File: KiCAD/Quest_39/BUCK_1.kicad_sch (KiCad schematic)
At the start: 21 parts

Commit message: Fixed most ERC errors
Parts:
- gave numbers to parts that had none: 21
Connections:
- net Vin-: now also C33.2, R15.2, U9.9 (Vin-)
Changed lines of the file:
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@@
     (effects (font (size 1.27 1.27)) (justify left bottom))
   )
-  (label "Vin-" (at 62.23 78.74 0)
+  (label "Vin-" (at 63.5 78.74 0)
     (effects (font (size 1.27 1.27)) (justify left bottom))
   )
@@
   (symbol (lib_id "Device:C") (at 127 137.16 0) (unit 1)
     (in_bom yes) (on_board yes) (fields_autoplaced)
-    (property "Reference" "C?" (id 0) (at 130.81 135.8899 0)
+    (property "Reference" "C34" (id 0) (at 130.81 135.8899 0)
       (effects (font (size 1.27 1.27)) (justify left))
     )
@@
   (symbol (lib_id "power:+5V") (at 77.47 59.69 0) (unit 1)
     (in_bom yes) (on_board yes) (fields_autoplaced)
-    (property "Reference" "#PWR0120" (id 0) (at 77.47 63.5 0)
+    (property "Reference" "#PWR015" (id 0) (at 77.47 63.5 0)
       (effects (font (size 1.27 1.27)) hide)
     )
@@
   (symbol (lib_id "Device:C_Polarized") (at 85.09 46.99 0) (unit 1)
     (in_bom yes) (on_board yes) (fields_autoplaced)
-    (property "Reference" "C?" (id 0) (at 88.9 44.8309 0)
+    (property "Reference" "C29" (id 0) (at 88.9 44.8309 0)
       (effects (font (size 1.27 1.27)) (justify left))
     )
@@
   (symbol (lib_id "Device:R") (at 46.99 49.53 0) (unit 1)
     (in_bom yes) (on_board yes) (fields_autoplaced)
-    (property "Reference" "R?" (id 0) (at 49.53 48.2599 0)
+    (property "Reference" "R14" (id 0) (at 49.53 48.2599 0)
       (effects (font (size 1.27 1.27)) (justify left))
     )
@@
   (symbol (lib_id "Amplifier_Operational:MCP601-xOT") (at 34.29 66.04 0) (unit 1)
     (in_bom yes) (on_board yes)
-    (property "Reference" "U?" (id 0) (at 36.83 62.23 0))
+    (property "Reference" "U8" (id 0) (at 36.83 62.23 0))
     (property "Value" "MCP601T-I/OT" (id 1) (at 40.64 69.85 0))
     (property "Footprint" "Package_TO_SOT_SMD:SOT-23-5" (id 2) (at 31.75 71.12 0)
@@
   (symbol (lib_id "power:GND") (at 281.94 229.87 0) (unit 1)
     (in_bom yes) (on_board yes) (fields_autoplaced)
-    (property "Reference" "#PWR0117" (id 0) (at 281.94 236.22 0)
+    (property "Reference" "#PWR019" (id 0) (at 281.94 236.22 0)
       (effects (font (size 1.27 1.27)) hide)
     )
@@
   (symbol (lib_id "power:+5V") (at 336.55 218.44 0) (unit 1)
     (in_bom yes) (on_board yes) (fields_autoplaced)
-    (property "Reference" "#PWR0118" (id 0) (at 336.55 222.25 0)
+    (property "Reference" "#PWR018" (id 0) (at 336.55 222.25 0)
       (effects (font (size 1.27 1.27)) hide)
     )
@@
   (symbol (lib_id "Device:C") (at 99.06 46.99 0) (unit 1)
     (in_bom yes) (on_board yes) (fields_autoplaced)
-    (property "Reference" "C?" (id 0) (at 102.87 45.7199 0)
+    (property "Reference" "C30" (id 0) (at 102.87 45.7199 0)
       (effects (font (size 1.27 1.27)) (justify left))
     )
@@
   (symbol (lib_id "Device:C_Polarized") (at 353.06 172.72 0) (unit 1)
     (in_bom yes) (on_board yes)
-    (property "Reference" "C?" (id 0) (at 356.8495 171.4075 0)
+    (property "Reference" "C36" (id 0) (at 356.8495 171.4075 0)
       (effects (font (size 1.27 1.27)) (justify left))
     )
@@
   (symbol (lib_id "power:+5V") (at 31.75 57.15 0) (unit 1)
     (in_bom yes) (on_board yes) (fields_autoplaced)
-    (property "Reference" "#PWR0121" (id 0) (at 31.75 60.96 0)
+    (property "Reference" "#PWR014" (id 0) (at 31.75 60.96 0)
       (effects (font (size 1.27 1.27)) hide)
     )
@@
   (symbol (lib_id "Device:C") (at 54.61 55.88 90) (unit 1)
     (in_bom yes) (on_board yes)
-    (property "Reference" "C?" (id 0) (at 54.61 52.07 90))
+    (property "Reference" "C33" (id 0) (at 54.61 52.07 90))
     (property "Value" "1uF" (id 1) (at 54.61 59.69 90))
     (property "Footprint" "OptoDevice:R_LDR_4.9x4.2mm_P2.54mm_Vertical" (id 2) (at 58.42 54.9148 0)
@@
   (symbol (lib_id "Device:R") (at 125.73 91.44 0) (unit 1)
     (in_bom yes) (on_board yes) (fields_autoplaced)
-    (property "Reference" "R?" (id 0) (at 128.27 90.1699 0)
+    (property "Reference" "R16" (id 0) (at 128.27 90.1699 0)
       (effects (font (size 1.27 1.27)) (justify left))
     )
@@
   (symbol (lib_id "Device:R") (at 321.31 215.9 0) (unit 1)
     (in_bom yes) (on_board yes) (fields_autoplaced)
-    (property "Reference" "R?" (id 0) (at 323.85 214.6299 0)
+    (property "Reference" "R17" (id 0) (at 323.85 214.6299 0)
       (effects (font (size 1.27 1.27)) (justify left))
     )
@@
   (symbol (lib_id "Device:C_Polarized") (at 367.03 172.72 0) (unit 1)
     (in_bom yes) (on_board yes)
-    (property "Reference" "C?" (id 0) (at 370.8195 171.4075 0)
+    (property "Reference" "C37" (id 0) (at 370.8195 171.4075 0)
       (effects (font (size 1.27 1.27)) (justify left))
     )
@@
   (symbol (lib_id "LTM4611EV:LTM4611EV-PBF") (at 130.81 102.87 0) (unit 1)
     (in_bom yes) (on_board yes)
-    (property "Reference" "U?" (id 0) (at 307.34 50.8 0)
+    (property "Reference" "U10" (id 0) (at 307.34 50.8 0)
       (effects (font (size 1.524 1.524)))
     )
@@
   (symbol (lib_id "Device:R") (at 54.61 41.91 90) (unit 1)
     (in_bom yes) (on_board yes) (fields_autoplaced)
-    (property "Reference" "R?" (id 0) (at 54.61 35.56 90))
+    (property "Reference" "R13" (id 0) (at 54.61 35.56 90))
     (property "Value" "0R0025" (id 1) (at 54.61 38.1 90))
     (property "Footprint" "" (id 2) (at 54.61 43.688 90)
@@
   (symbol (lib_id "Analog_ADC:INA226") (at 77.47 73.66 0) (unit 1)
     (in_bom yes) (on_board yes)
-    (property "Reference" "U?" (id 0) (at 82.55 62.23 0)
+    (property "Reference" "U9" (id 0) (at 82.55 62.23 0)
       (effects (font (size 1.27 1.27)) (justify left))
     )
@@
   (symbol (lib_id "Device:C") (at 336.55 224.79 0) (unit 1)
     (in_bom yes) (on_board yes) (fields_autoplaced)
-    (property "Reference" "C?" (id 0) (at 340.36 223.5199 0)
+    (property "Reference" "C40" (id 0) (at 340.36 223.5199 0)
       (effects (font (size 1.27 1.27)) (justify left))
     )
@@
   (symbol (lib_id "power:GND") (at 31.75 76.2 0) (unit 1)
     (in_bom yes) (on_board yes) (fields_autoplaced)
-    (property "Reference" "#PWR0123" (id 0) (at 31.75 82.55 0)
+    (property "Reference" "#PWR016" (id 0) (at 31.75 82.55 0)
       (effects (font (size 1.27 1.27)) hide)
     )
@@
   (symbol (lib_id "Device:R") (at 59.69 49.53 0) (unit 1)
     (in_bom yes) (on_board yes) (fields_autoplaced)
-    (property "Reference" "R?" (id 0) (at 62.23 48.2599 0)
+    (property "Reference" "R15" (id 0) (at 62.23 48.2599 0)
       (effects (font (size 1.27 1.27)) (justify left))
     )
@@
   (symbol (lib_id "power:GND") (at 100.33 87.63 0) (unit 1)
     (in_bom yes) (on_board yes) (fields_autoplaced)
-    (property "Reference" "#PWR0122" (id 0) (at 100.33 93.98 0)
+    (property "Reference" "#PWR017" (id 0) (at 100.33 93.98 0)
       (effects (font (size 1.27 1.27)) hide)
     )
@@
   (symbol (lib_id "MCP4151:MCP4151-502E{slash}SN") (at 252.73 220.98 0) (unit 1)
     (in_bom yes) (on_board yes)
-    (property "Reference" "U?" (id 0) (at 311.15 214.63 0)
+    (property "Reference" "U11" (id 0) (at 311.15 214.63 0)
       (effects (font (size 1.524 1.524)))
     )
@@
   (symbol (lib_id "Device:C_Polarized") (at 379.73 172.72 0) (unit 1)
     (in_bom yes) (on_board yes)
-    (property "Reference" "C?" (id 0) (at 383.5195 171.4075 0)
+    (property "Reference" "C38" (id 0) (at 383.5195 171.4075 0)
       (effects (font (size 1.27 1.27)) (justify left))
     )
@@
   (symbol (lib_id "Device:C") (at 111.76 46.99 0) (unit 1)
     (in_bom yes) (on_board yes) (fields_autoplaced)
-    (property "Reference" "C?" (id 0) (at 115.57 45.7199 0)
+    (property "Reference" "C31" (id 0) (at 115.57 45.7199 0)
       (effects (font (size 1.27 1.27)) (justify left))
     )
@@
   (symbol (lib_id "Device:C") (at 334.01 172.72 0) (unit 1)
     (in_bom yes) (on_board yes) (fields_autoplaced)
-    (property "Reference" "C?" (id 0) (at 337.82 171.4499 0)
+    (property "Reference" "C35" (id 0) (at 337.82 171.4499 0)
       (effects (font (size 1.27 1.27)) (justify left))
     )
@@
   (symbol (lib_id "Device:C_Polarized") (at 392.43 172.72 0) (unit 1)
     (in_bom yes) (on_board yes)
-    (property "Reference" "C?" (id 0) (at 396.2195 171.4075 0)
+    (property "Reference" "C39" (id 0) (at 396.2195 171.4075 0)
       (effects (font (size 1.27 1.27)) (justify left))
     )
@@
   (symbol (lib_id "power:GND") (at 336.55 229.87 0) (unit 1)
     (in_bom yes) (on_board yes) (fields_autoplaced)
-    (property "Reference" "#PWR0119" (id 0) (at 336.55 236.22 0)
+    (property "Reference" "#PWR020" (id 0) (at 336.55 236.22 0)
       (effects (font (size 1.27 1.27)) hide)
     )
@@
   (symbol (lib_id "Device:C") (at 124.46 46.99 0) (unit 1)
     (in_bom yes) (on_board yes) (fields_autoplaced)
-    (property "Reference" "C?" (id 0) (at 128.27 45.7199 0)
-      (effects (font (size 1.27 1.27)) (justify left))
-    )
+    (property "Reference" "C32" (id 0) (at 128.27 45.7199 0)
+      (effects (font (size 1.27 1.27)) (justify left))
+    )

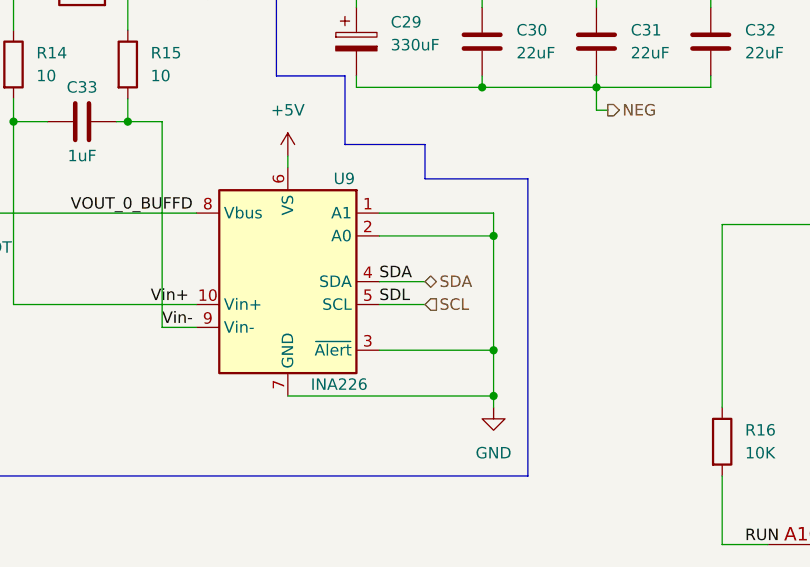
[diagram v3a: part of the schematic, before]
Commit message: Added weak SPI CS pullups to prevent spurious behaviour
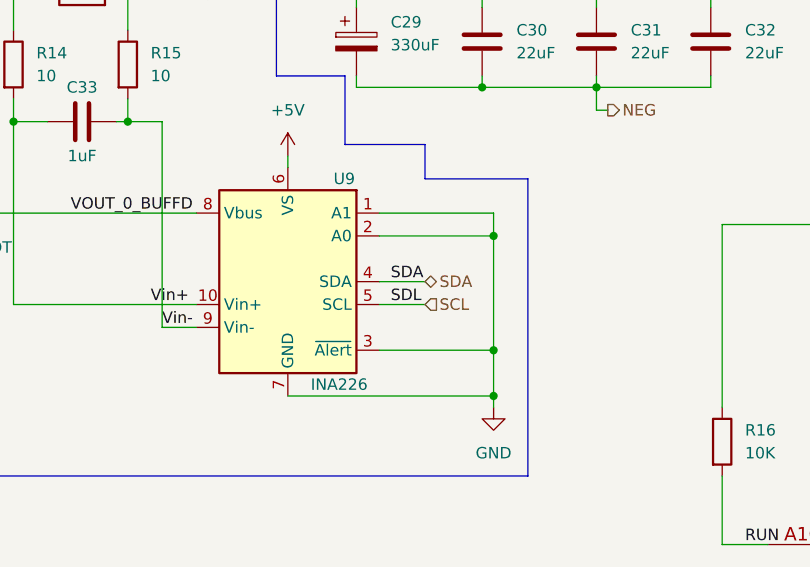
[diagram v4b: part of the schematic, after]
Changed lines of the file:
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@@
+    (effects (font (size 1.27 1.27)) (justify left bottom))
+  )
+  (label "SDA" (at 88.9 73.66 0)
     (effects (font (size 1.27 1.27)) (justify left bottom))
   )
@@
     (effects (font (size 1.27 1.27)) (justify left bottom))
   )
-  (label "SDL" (at 87.63 76.2 0)
+  (label "VOUT_0_BUFFD" (at 53.34 66.04 0)
     (effects (font (size 1.27 1.27)) (justify left bottom))
   )
-  (label "VOUT_0_BUFFD" (at 53.34 66.04 0)
+  (label "SDL" (at 88.9 76.2 0)
     (effects (font (size 1.27 1.27)) (justify left bottom))
   )
@@
     (effects (font (size 1.27 1.27)) (justify left bottom))
   )
-  (label "SDA" (at 87.63 73.66 0)
-    (effects (font (size 1.27 1.27)) (justify left bottom))
-  )

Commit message: Gave all INA226's unique addresses
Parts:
- removed C29: 330uF, symbol Device:C_Polarized
- removed R13: 0R0025, symbol Device:R
- removed R14, R15: 10, symbol Device:R
- removed R16: 10K, symbol Device:R
- removed R17: 20K, symbol Device:R
- removed U8: MCP601T-I/OT, Package_TO_SOT_SMD:SOT-23-5, symbol Amplifier_Operational:MCP601-xOT
- added C28: 330uF, symbol Device:C_Polarized
- added C29: 22uF, symbol Device:C
- added C41: 100nF, symbol Device:C
- added R24: 0R0025, symbol Device:R
- added R25, R26: 10R, symbol Device:R
- added R27: 9k, symbol Device:R
- added R28: 1k, symbol Device:R
- added R29: 10k, symbol Device:R
- added R30: 20K, symbol Device:R
- added TP13, TP14, TP15, TP16, TP17, TP18, TP19: TestPoint, symbol Connector:TestPoint
- added U8: AD626ANZ, N_8_ADI, symbol AD626ANZ:AD626ANZ
- C32: value 22uF -> 1uF; footprint (none) -> OptoDevice:R_LDR_4.9x4.2mm_P2.54mm_Vertical
- C33: value 1uF -> 100nF; footprint OptoDevice:R_LDR_4.9x4.2mm_P2.54mm_Vertical -> (none)
- C35: value 100pF -> 10nF
- C40: value 100nF -> 100pF
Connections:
- net +5V: now also C34.1, U9.2 (A0), C41.1, U8.6 (+VS); no longer C40.1
- net GND: now also C33.2, C34.2, C41.2, U8.2 (AGND), U8.3 (-VS); no longer C40.2, U9.2 (A0), U9.3 (~{Alert})
- net NEG: now also C35.1, C28.2, C29.2, R28.2, U8.1 (-IN); no longer C32.2, C34.2, U9.8 (Vbus)
- net P0A: now also R30.2
- net POS: now also C40.1; no longer C35.1
- net PV_POS: now also C30.1, C31.1, U10.A1 (VIN), U10.A2 (VIN), U10.A3 (VIN), U10.A4 (VIN), U10.A5 (VIN), U10.A6 (VIN), U10.B1 (VIN), U10.B2 (VIN), U10.B3 (VIN), U10.B4 (VIN), U10.B5 (VIN), U10.B6 (VIN), U10.C1 (VIN), U10.C2 (VIN), U10.C3 (VIN), U10.C4 (VIN), U10.C5 (VIN), U10.C6 (VIN), C28.1, C29.1, R24.1, R24.2, R25.1, R26.1, R27.1, R29.1
- net RUN: now also R29.2
- net TRACK/SS: now also C35.2; no longer C34.1
- net Vfb: now also C40.2, R30.1; no longer C35.2
- net Vin+: now also C32.1, R25.2; no longer C33.1
- net Vin-: now also C32.2, U9.8 (Vbus), R26.2, TP14.1, U8.5 (OUT); no longer C33.2
- net at U10.A11 (COMP): now also TP17.1
- net at U10.A7 (INTVCC): now also U10.D9 (INTVCC), TP13.1
- net at U10.B12 (PLLFLTR/FSET): now also TP16.1
- net at U10.F11 (PGOOD): now also U10.G12 (PGOOD), TP15.1
- net at U10.K12 (DIFFVOUT), U10.L12 (VOUT_LCL): now also TP18.1, TP19.1
- new net: C33.1, U8.4 (FILTER)
- new net +IN: R27.2, R28.1, U8.8 (+IN)
- no-connect marks 16 -> 12
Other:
- note added: "10:1 divider"
- note added: "Addr=0x41"
- note added: "Extra mounting"
- note added: "G=10"
- note added: "Output voltage is set by varying Rfb with a digipot. SPI = 00"
- note added: "the measured voltage is divided and then amplified by 10 as to simulate a follower. This is done to make use of the AD626 (low price and availability)."

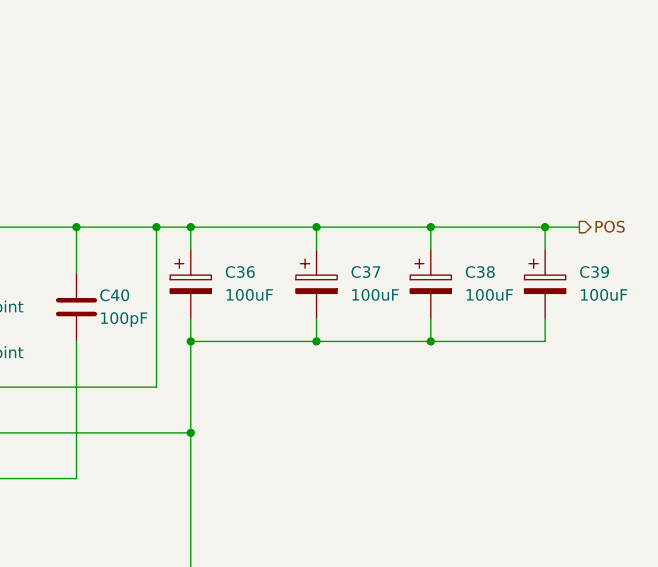
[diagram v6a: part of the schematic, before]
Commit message: Assigned all schem. symbols their footprints
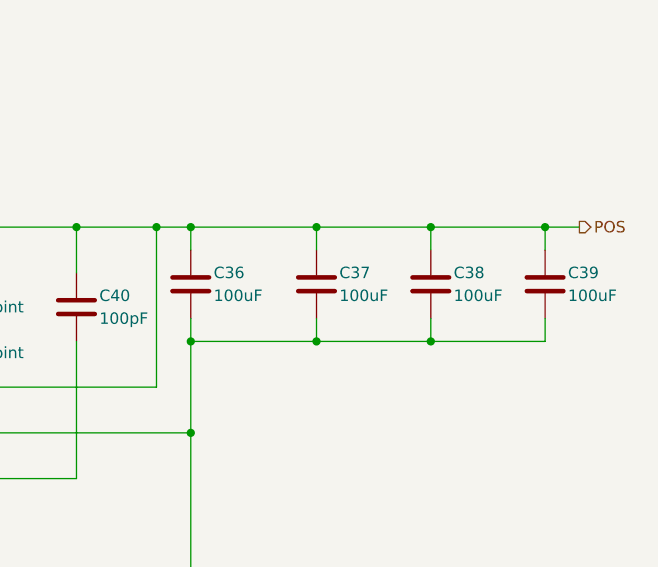
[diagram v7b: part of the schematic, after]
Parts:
- removed C36, C37, C38, C39: 100uF, symbol Device:C_Polarized
- added C36, C37, C38, C39: 100uF, Capacitor_SMD:C_1206_3216Metric, symbol Device:C
- C28: footprint (none) -> Capacitor_SMD:CP_Elec_8x6.9
- C29, C30, C31, C33, C34, C35, C40, C41: footprint (none) -> Capacitor_SMD:C_0805_2012Metric
- C32: footprint OptoDevice:R_LDR_4.9x4.2mm_P2.54mm_Vertical -> Capacitor_SMD:C_0805_2012Metric
- R24: footprint (none) -> Resistor_SMD:R_1206_3216Metric
- R25, R26, R27, R28, R29, R30: footprint (none) -> Resistor_SMD:R_0805_2012Metric
- TP13, TP14, TP15, TP16, TP17, TP18, TP19: footprint (none) -> TestPoint:TestPoint_Pad_D2.0mm
- U10: footprint LGA-133_3_LIT -> Package_LGA:Linear_LGA-133_15.0x15.0mm_Layout12x12_P1.27mm
- U11: footprint SOIC8-N_MC_MCH -> Package_SO:MSOP-8_3x3mm_P0.65mm
- U8: footprint N_8_ADI -> Package_DIP:DIP-8_W7.62mm_Socket_LongPads
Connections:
- net NEG: now also C36.2, C37.2, C38.2, C39.2
- net POS: now also C36.1, C37.1, C38.1, C39.1

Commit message: Initial work on layout
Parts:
- C32, C33, C34, C35, C40, C41: footprint Capacitor_SMD:C_0805_2012Metric -> Capacitor_SMD:C_0603_1608Metric
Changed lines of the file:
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@@
       (effects (font (size 1.27 1.27)) (justify left))
     )
-    (property "Footprint" "Capacitor_SMD:C_0805_2012Metric" (id 2) (at 64.4652 88.9 0)
+    (property "Footprint" "Capacitor_SMD:C_0603_1608Metric" (id 2) (at 64.4652 88.9 0)
       (effects (font (size 1.27 1.27)) hide)
     )
@@
       (effects (font (size 1.27 1.27)) (justify left))
     )
-    (property "Footprint" "Capacitor_SMD:C_0805_2012Metric" (id 2) (at 341.3252 227.33 0)
+    (property "Footprint" "Capacitor_SMD:C_0603_1608Metric" (id 2) (at 341.3252 227.33 0)
       (effects (font (size 1.27 1.27)) hide)
     )
@@
       (effects (font (size 1.27 1.27)) (justify left))
     )
-    (property "Footprint" "Capacitor_SMD:C_0805_2012Metric" (id 2) (at 26.3652 87.63 0)
+    (property "Footprint" "Capacitor_SMD:C_0603_1608Metric" (id 2) (at 26.3652 87.63 0)
       (effects (font (size 1.27 1.27)) hide)
     )
@@
       (effects (font (size 1.27 1.27)) (justify left))
     )
-    (property "Footprint" "Capacitor_SMD:C_0805_2012Metric" (id 2) (at 106.3752 130.81 0)
+    (property "Footprint" "Capacitor_SMD:C_0603_1608Metric" (id 2) (at 106.3752 130.81 0)
       (effects (font (size 1.27 1.27)) hide)
     )
@@
     (property "Reference" "C32" (id 0) (at 74.93 63.5 90))
     (property "Value" "1uF" (id 1) (at 74.93 71.12 90))
-    (property "Footprint" "Capacitor_SMD:C_0805_2012Metric" (id 2) (at 78.74 66.3448 0)
+    (property "Footprint" "Capacitor_SMD:C_0603_1608Metric" (id 2) (at 78.74 66.3448 0)
       (effects (font (size 1.27 1.27)) hide)
     )
@@
       (effects (font (size 1.27 1.27)) (justify left))
     )
-    (property "Footprint" "Capacitor_SMD:C_0805_2012Metric" (id 2) (at 345.1352 175.26 0)
-      (effects (font (size 1.27 1.27)) hide)
-    )
+    (property "Footprint" "Capacitor_SMD:C_0603_1608Metric" (id 2) (at 345.1352 175.26 0)
+      (effects (font (size 1.27 1.27)) hide)
+    )
